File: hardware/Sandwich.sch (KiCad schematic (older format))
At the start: 2 parts

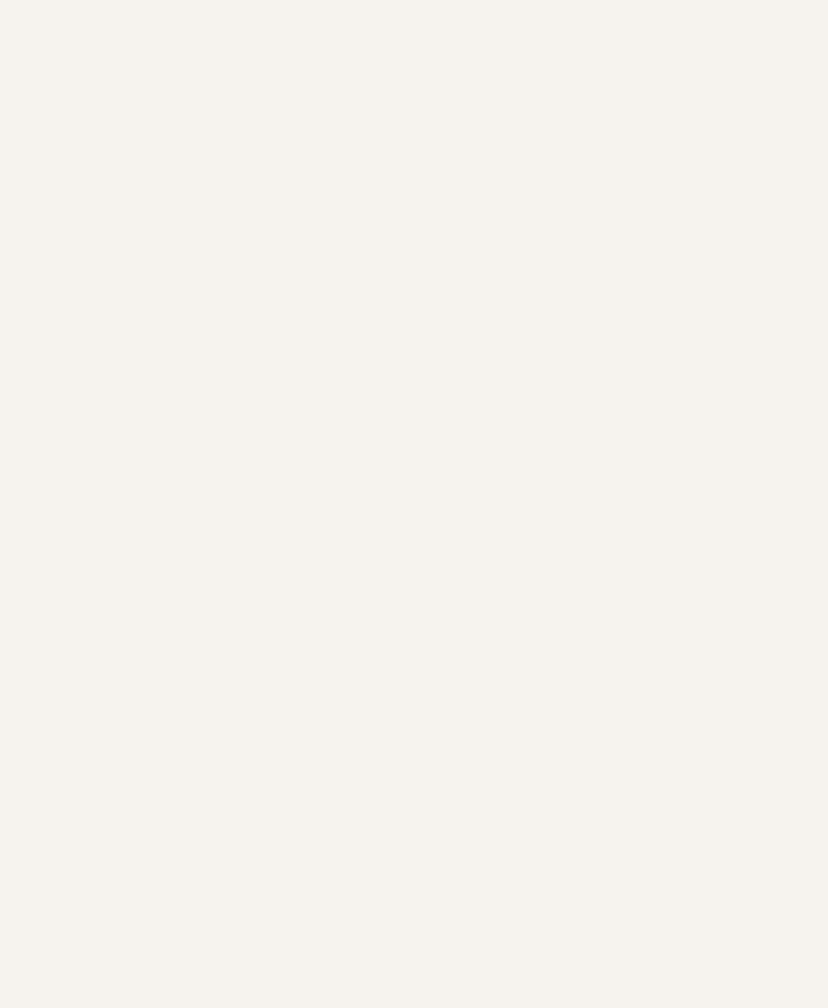
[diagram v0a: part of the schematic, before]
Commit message: Started working on the VGA interface.
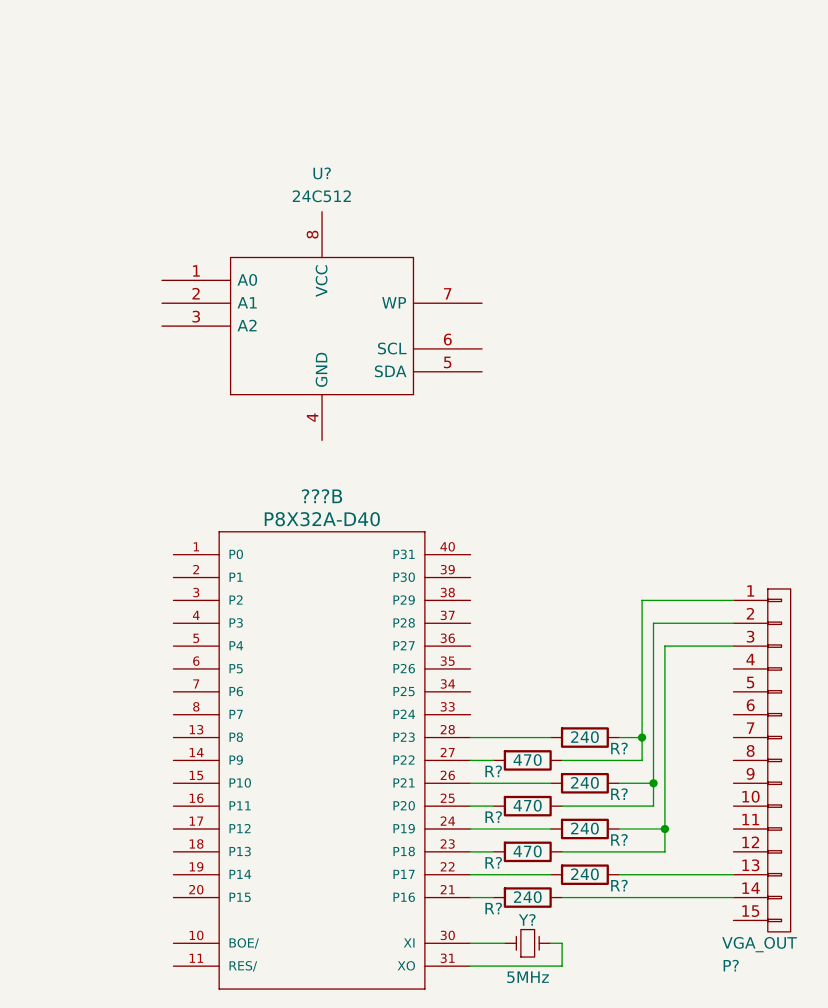
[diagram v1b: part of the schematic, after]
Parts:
- added ???: P8X32A-D40, symbol P8X32A-D40
- added P?: VGA_OUT, symbol CONN_01X15
- added R? (x5): 240, symbol R
- added R? (x3): 470, symbol R
- added U?: 24C512, symbol 24C512
- added Y?: 5MHz, symbol Crystal_Small
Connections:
- new net: ???.21 (P16), R?.2
- new net: ???.22 (P17), R?.2
- new net: ???.23 (P18), R?.2
- new net: ???.24 (P19), R?.2
- new net: ???.25 (P20), R?.2
- new net: ???.26 (P21), R?.2
- new net: ???.27 (P22), R?.2
- new net: ???.28 (P23), R?.2
- new net: ???.30 (XI), Y?.1
- new net: ???.31 (XO), Y?.2
- new net: P?.1 (P1), R?.1, R?.1
- new net: P?.13 (P13), R?.1
- new net: P?.14 (P14), R?.1
- new net: P?.2 (P2), R?.1, R?.1
- new net: P?.3 (P3), R?.1, R?.1
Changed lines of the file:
@@
 LIBS:valves
 LIBS:Zilog
+LIBS:parallax_propeller
+LIBS:Sandwich-cache
 EELAYER 25 0
 EELAYER END
@@
 Wire Wire Line
 	2100 5200 2300 5200
+$Comp
+L P8X32A-D40 ???
+U 2 1 56B3D7DA
+P 9050 4650
+F 0 "???" H 9100 5703 60  0000 C CNN
+F 1 "P8X32A-D40" H 9100 5603 60  0000 C CNN
+F 2 "" H 9050 4650 60  0000 C CNN
+F 3 "" H 9050 4650 60  0000 C CNN
+	2    9050 4650
+	1    0    0    -1
+$EndComp
+$Comp
+L CONN_01X15 P?
+U 1 1 56B3D8DB
+P 11100 4750
+F 0 "P?" H 10850 3850 50  0000 L CNN
+F 1 "VGA_OUT" H 10850 3950 50  0000 L CNN
+F 2 "" H 11100 4750 50  0000 C CNN
+F 3 "" H 11100 4750 50  0000 C CNN
+	1    11100 4750
+	1    0    0    -1
+$EndComp
+$Comp
+L R R?
+U 1 1 56B3DA31
+P 10000 5350
+F 0 "R?" V 10050 5200 50  0000 C CNN
+F 1 "240" V 10000 5350 50  0000 C CNN
+F 2 "" V 9930 5350 50  0000 C CNN
+F 3 "" H 10000 5350 50  0000 C CNN
+	1    10000 5350
+	0    1    1    0
+$EndComp
+$Comp
+L R R?
+U 1 1 56B3DA8C
+P 10250 5250
+F 0 "R?" V 10300 5400 50  0000 C CNN
+F 1 "240" V 10250 5250 50  0000 C CNN
+F 2 "" V 10180 5250 50  0000 C CNN
+F 3 "" H 10250 5250 50  0000 C CNN
+	1    10250 5250
+	0    1    1    0
+$EndComp
+Wire Wire Line
+	9750 5350 9850 5350
+Wire Wire Line
+	9750 5250 10100 5250
+$Comp
+L R R?
+U 1 1 56B3DB9A
+P 10000 5150
+F 0 "R?" V 10050 5000 50  0000 C CNN
+F 1 "470" V 10000 5150 50  0000 C CNN
+F 2 "" V 9930 5150 50  0000 C CNN
+F 3 "" H 10000 5150 50  0000 C CNN
+	1    10000 5150
+	0    1    1    0
+$EndComp
+$Comp
+L R R?
+U 1 1 56B3DBE5
+P 10250 5050
+F 0 "R?" V 10300 5200 50  0000 C CNN
+F 1 "240" V 10250 5050 50  0000 C CNN
+F 2 "" V 10180 5050 50  0000 C CNN
+F 3 "" H 10250 5050 50  0000 C CNN
+	1    10250 5050
+	0    1    1    0
+$EndComp
+Wire Wire Line
+	9850 5150 9750 5150
+Wire Wire Line
+	9750 5050 10100 5050
+$Comp
+L R R?
+U 1 1 56B3DEC9
+P 10000 4950
+F 0 "R?" V 10050 4800 50  0000 C CNN
+F 1 "470" V 10000 4950 50  0000 C CNN
+F 2 "" V 9930 4950 50  0000 C CNN
+F 3 "" H 10000 4950 50  0000 C CNN
+	1    10000 4950
+	0    1    1    0
+$EndComp
+$Comp
+L R R?
+U 1 1 56B3DF20
+P 10250 4850
+F 0 "R?" V 10300 5000 50  0000 C CNN
+F 1 "240" V 10250 4850 50  0000 C CNN
+F 2 "" V 10180 4850 50  0000 C CNN
+F 3 "" H 10250 4850 50  0000 C CNN
+	1    10250 4850
+	0    1    1    0
+$EndComp
+Wire Wire Line
+	9750 4950 9850 4950
+Wire Wire Line
+	10100 4850 9750 4850
+$Comp
+L R R?
+U 1 1 56B3E13C
+P 10000 4750
+F 0 "R?" V 10050 4600 50  0000 C CNN
+F 1 "470" V 10000 4750 50  0000 C CNN
+F 2 "" V 9930 4750 50  0000 C CNN
+F 3 "" H 10000 4750 50  0000 C CNN
+	1    10000 4750
+	0    1    1    0
+$EndComp
+$Comp
+L R R?
+U 1 1 56B3E18E
+P 10250 4650
+F 0 "R?" V 10300 4800 50  0000 C CNN
+F 1 "240" V 10250 4650 50  0000 C CNN
+F 2 "" V 10180 4650 50  0000 C CNN
+F 3 "" H 10250 4650 50  0000 C CNN
+	1    10250 4650
+	0    1    1    0
+$EndComp
+Wire Wire Line
+	9850 4750 9750 4750
+Wire Wire Line
+	9750 4650 10100 4650
+Wire Wire Line
+	10400 5250 10900 5250
+Wire Wire Line
+	10900 5350 10150 5350
+Wire Wire Line
+	10150 5150 10600 5150
+Wire Wire Line
+	10600 5150 10600 4250
+Wire Wire Line
+	10600 4250 10900 4250
+Wire Wire Line
+	10400 5050 10600 5050
+Connection ~ 10600 5050
+Wire Wire Line
+	10150 4950 10550 4950
+Wire Wire Line
+	10550 4950 10550 4150
+Wire Wire Line
+	10550 4150 10900 4150
+Wire Wire Line
+	10400 4850 10550 4850
+Connection ~ 10550 4850
+Wire Wire Line
+	10150 4750 10500 4750
+Wire Wire Line
+	10500 4750 10500 4050
+Wire Wire Line
+	10500 4050 10900 4050
+Wire Wire Line
+	10400 4650 10500 4650
+Connection ~ 10500 4650
+$Comp
+L Crystal_Small Y?
+U 1 1 56B3E76F
+P 10000 5550
+F 0 "Y?" H 10000 5650 50  0000 C CNN
+F 1 "5MHz" H 10000 5400 50  0000 C CNN
+F 2 "" H 10000 5550 50  0000 C CNN
+F 3 "" H 10000 5550 50  0000 C CNN
+	1    10000 5550
+	1    0    0    -1
+$EndComp
+Wire Wire Line
+	9750 5550 9900 5550
+Wire Wire Line
+	9750 5650 10150 5650
+Wire Wire Line
+	10150 5650 10150 5550
+Wire Wire Line
+	10150 5550 10100 5550
+$Comp
+L 24C512 U?
+U 1 1 56B3EA78
+P 9100 2850
+F 0 "U?" H 9100 3516 50  0000 C CNN
+F 1 "24C512" H 9100 3416 50  0000 C CNN
+F 2 "" H 9100 2850 50  0000 C CNN
+F 3 "" H 9100 2850 50  0000 C CNN
+	1    9100 2850
+	1    0    0    -1
+$EndComp
 $EndSCHEMATC

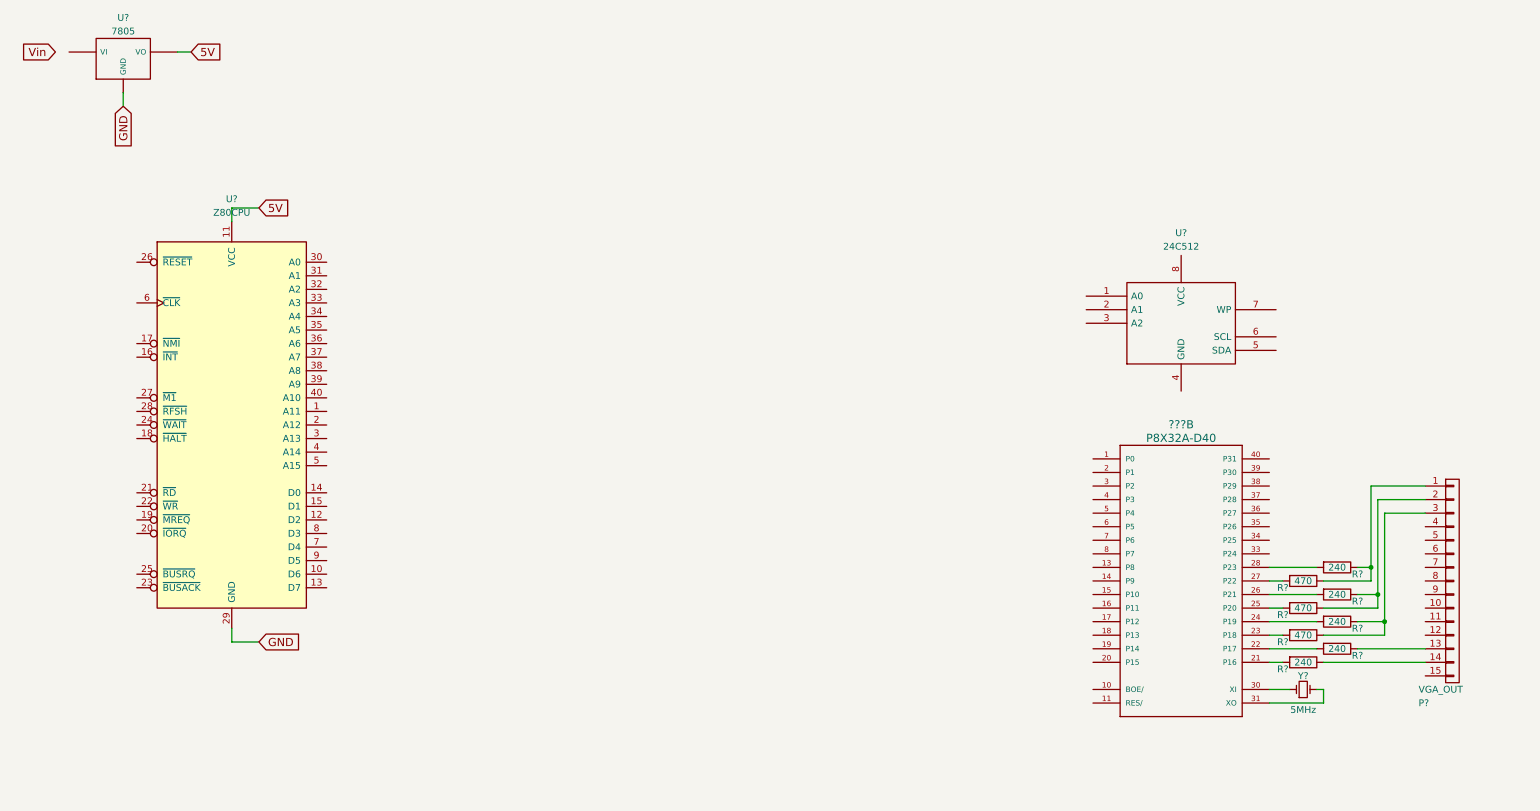
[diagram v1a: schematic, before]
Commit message: Added a circuit for resetting the Propeller for programming when DTR gets activated.
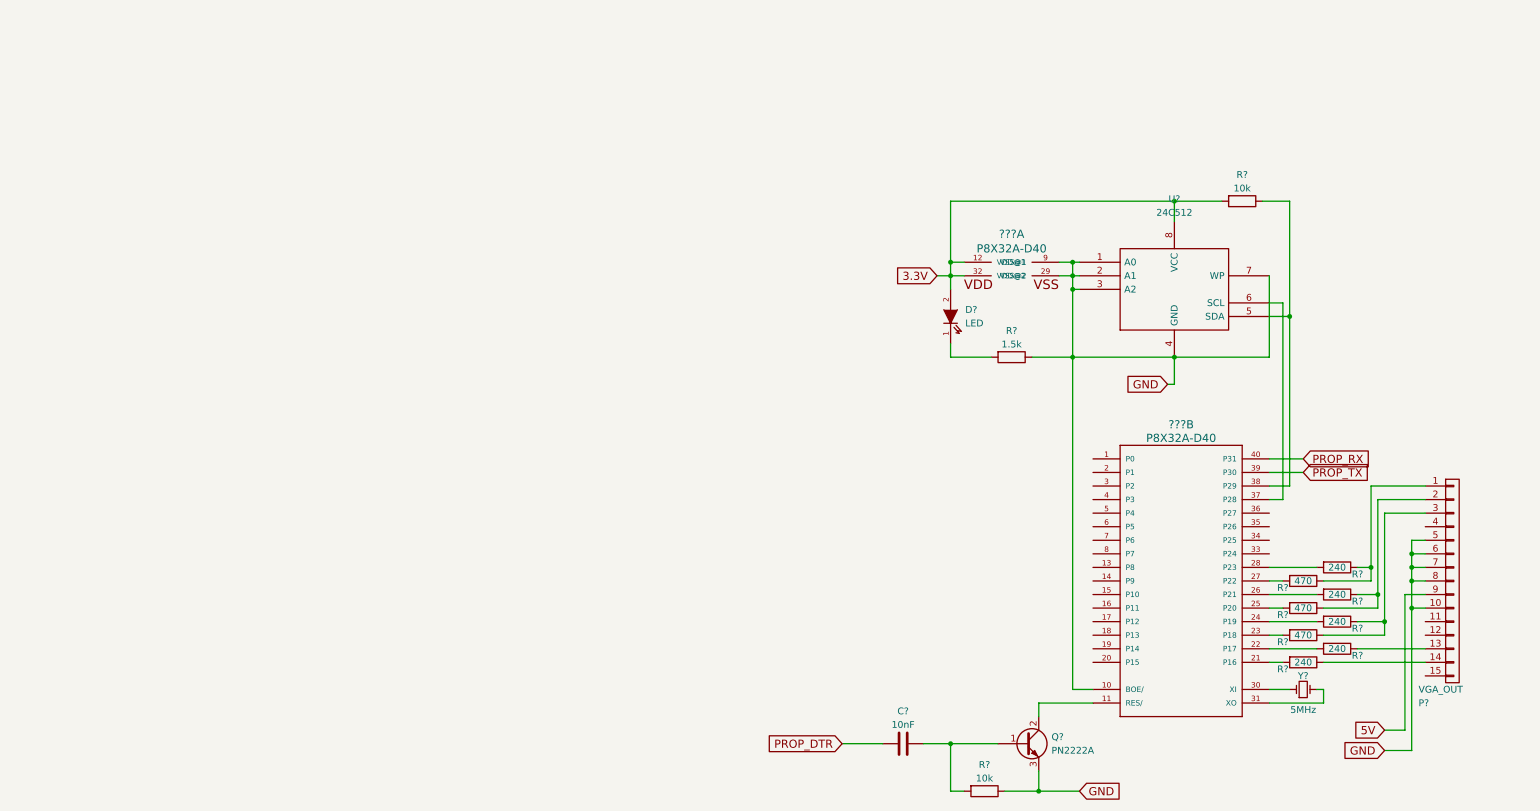
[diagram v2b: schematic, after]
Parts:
- removed U?: Z80CPU, symbol Z80CPU
- removed U?: 7805, symbol 7805
- added ???: P8X32A-D40, symbol P8X32A-D40
- added C?: 10nF, symbol C
- added D?: LED, symbol LED
- added Q?: PN2222A, symbol Q_NPN_BCE
- added R? (x2): 10k, symbol R
- added R?: 1.5k, symbol R
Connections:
- net 5V: now also P?.9 (P9)
- net GND: now also ???.10 (BOE/), P?.10 (P10), P?.5 (P5), P?.6 (P6), P?.7 (P7), P?.8 (P8), U?.1 (A0), U?.2 (A1), U?.3 (A2), U?.4 (GND), U?.7 (WP), ???.29 (VSS@2), ???.9 (VSS@1), Q?.3 (E), R?.1, R?.1
- net at ???.11 (RES/): now also Q?.2 (C)
- net at ???.37 (P28): now also U?.6 (SCL)
- net at ???.38 (P29): now also U?.5 (SDA), R?.1
- net PROP_TX: now reaches ???.39 (P30)
- net PROP_RX: now reaches ???.40 (P31)
- net 3.3V: now reaches U?.8 (VCC)
- net 3.3V: now also ???.12 (VDD@1), ???.32 (VDD@2), D?.2 (A), R?.2
- new net: D?.1 (K), R?.2
- new net: C?.1, Q?.1 (B), R?.2
- new net PROP_DTR: C?.2
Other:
- moved on the sheet: U?
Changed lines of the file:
@@
 $EndDescr
-$Comp
-L Z80CPU U?
-U 1 1 56AFD33E
-P 2100 3600
-F 0 "U?" H 2100 5266 50  0000 C CNN
-F 1 "Z80CPU" H 2100 5166 50  0000 C CNN
-F 2 "" H 2100 4000 50  0000 C CNN
-F 3 "" H 2100 4000 50  0000 C CNN
-	1    2100 3600
-	1    0    0    -1
-$EndComp
-$Comp
-L 7805 U?
-U 1 1 56AFD55A
-P 1300 900
-F 0 "U?" H 1300 1203 50  0000 C CNN
-F 1 "7805" H 1300 1103 50  0000 C CNN
-F 2 "" H 1300 900 50  0000 C CNN
-F 3 "" H 1300 900 50  0000 C CNN
-	1    1300 900
-	1    0    0    -1
-$EndComp
-Text GLabel 1800 850  2    60   Input ~ 0
-5V
-Text GLabel 1300 1250 3    60   Input ~ 0
-GND
-Text GLabel 800  850  0    60   Input ~ 0
-Vin
-Wire Wire Line
-	1700 850  1800 850
-Wire Wire Line
-	1300 1250 1300 1150
-Text GLabel 2300 2000 2    60   Input ~ 0
-5V
-Wire Wire Line
-	2100 2100 2100 2000
-Wire Wire Line
-	2100 2000 2300 2000
-Text GLabel 2300 5200 2    60   Input ~ 0
-GND
-Wire Wire Line
-	2100 5100 2100 5200
-Wire Wire Line
-	2100 5200 2300 5200
 $Comp
 L P8X32A-D40 ???
@@
 L 24C512 U?
 U 1 1 56B3EA78
-P 9100 2850
-F 0 "U?" H 9100 3516 50  0000 C CNN
-F 1 "24C512" H 9100 3416 50  0000 C CNN
-F 2 "" H 9100 2850 50  0000 C CNN
-F 3 "" H 9100 2850 50  0000 C CNN
-	1    9100 2850
-	1    0    0    -1
-$EndComp
+P 9050 2600
+F 0 "U?" H 9050 3266 50  0000 C CNN
+F 1 "24C512" H 9050 3166 50  0000 C CNN
+F 2 "" H 9050 2600 50  0000 C CNN
+F 3 "" H 9050 2600 50  0000 C CNN
+	1    9050 2600
+	1    0    0    -1
+$EndComp
+$Comp
+L P8X32A-D40 ???
+U 1 1 56B5DEF4
+P 7900 2600
+F 0 "???" H 7850 3008 60  0000 C CNN
+F 1 "P8X32A-D40" H 7850 2900 60  0000 C CNN
+F 2 "" H 7900 2600 60  0000 C CNN
+F 3 "" H 7900 2600 60  0000 C CNN
+	1    7900 2600
+	1    0    0    -1
+$EndComp
+Wire Wire Line
+	8350 2400 8200 2400
+Wire Wire Line
+	8200 2500 8350 2500
+Wire Wire Line
+	8000 3100 9750 3100
+Wire Wire Line
+	8300 2400 8300 5550
+Connection ~ 8300 2500
+Connection ~ 8300 2400
+Wire Wire Line
+	8350 2600 8300 2600
+Connection ~ 8300 2600
+Wire Wire Line
+	7300 2500 7500 2500
+Wire Wire Line
+	7400 1950 9400 1950
+Wire Wire Line
+	7500 2400 7400 2400
+Connection ~ 7400 2400
+Text GLabel 10600 6000 0    60   Input ~ 0
+GND
+Wire Wire Line
+	10600 6000 10800 6000
+Wire Wire Line
+	10800 6000 10800 4450
+Wire Wire Line
+	10800 4450 10900 4450
+Wire Wire Line
+	10900 4550 10800 4550
+Connection ~ 10800 4550
+Wire Wire Line
+	10900 4650 10800 4650
+Connection ~ 10800 4650
+Wire Wire Line
+	10900 4750 10800 4750
+Connection ~ 10800 4750
+Wire Wire Line
+	10900 4950 10800 4950
+Connection ~ 10800 4950
+Text GLabel 10600 5850 0    60   Input ~ 0
+5V
+Wire Wire Line
+	10600 5850 10750 5850
+Wire Wire Line
+	10750 5850 10750 4850
+Wire Wire Line
+	10750 4850 10900 4850
+$Comp
+L R R?
+U 1 1 56B5E9EC
+P 9550 1950
+F 0 "R?" V 9355 1950 50  0000 C CNN
+F 1 "10k" V 9455 1950 50  0000 C CNN
+F 2 "" V 9480 1950 50  0000 C CNN
+F 3 "" H 9550 1950 50  0000 C CNN
+	1    9550 1950
+	0    1    1    0
+$EndComp
+Connection ~ 9050 1950
+Wire Wire Line
+	9900 1950 9900 4050
+Wire Wire Line
+	9900 2800 9750 2800
+Wire Wire Line
+	9900 4050 9750 4050
+Connection ~ 9900 2800
+Wire Wire Line
+	9750 2700 9850 2700
+Wire Wire Line
+	9850 2700 9850 4150
+Wire Wire Line
+	9850 4150 9750 4150
+Wire Wire Line
+	9700 1950 9900 1950
+Connection ~ 7400 2500
+Text GLabel 9000 3300 0    60   Input ~ 0
+GND
+Wire Wire Line
+	9000 3300 9050 3300
+Wire Wire Line
+	9050 3300 9050 3100
+Text GLabel 7300 2500 0    60   Input ~ 0
+3.3V
+Wire Wire Line
+	7400 1950 7400 2600
+$Comp
+L LED D?
+U 1 1 56B5F331
+P 7400 2800
+F 0 "D?" V 7450 2692 50  0000 R CNN
+F 1 "LED" V 7350 2692 50  0000 R CNN
+F 2 "" H 7400 2800 50  0000 C CNN
+F 3 "" H 7400 2800 50  0000 C CNN
+	1    7400 2800
+	0    -1   -1   0
+$EndComp
+$Comp
+L R R?
+U 1 1 56B5F44A
+P 7850 3100
+F 0 "R?" V 7655 3100 50  0000 C CNN
+F 1 "1.5k" V 7755 3100 50  0000 C CNN
+F 2 "" V 7780 3100 50  0000 C CNN
+F 3 "" H 7850 3100 50  0000 C CNN
+	1    7850 3100
+	0    1    1    0
+$EndComp
+Wire Wire Line
+	7400 3000 7400 3100
+Wire Wire Line
+	7400 3100 7700 3100
+Connection ~ 8300 3100
+Wire Wire Line
+	9050 2100 9050 1950
+Wire Wire Line
+	9750 3100 9750 2500
+Connection ~ 9050 3100
+Text GLabel 10000 3850 2    60   Input ~ 0
+PROP_RX
+Text GLabel 10000 3950 2    60   Input ~ 0
+PROP_TX
+Wire Wire Line
+	10000 3850 9750 3850
+Wire Wire Line
+	9750 3950 10000 3950
+Wire Wire Line
+	8300 5550 8450 5550
+$Comp
+L R R?
+U 1 1 56B7C3FF
+P 7650 6300
+F 0 "R?" V 7455 6300 50  0000 C CNN
+F 1 "10k" V 7555 6300 50  0000 C CNN
+F 2 "" V 7580 6300 50  0000 C CNN
+F 3 "" H 7650 6300 50  0000 C CNN
+	1    7650 6300
+	0    1    1    0
+$EndComp
+$Comp
+L Q_NPN_BCE Q?
+U 1 1 56B7C5EC
+P 7950 5950
+F 0 "Q?" H 8144 6000 50  0000 L CNN
+F 1 "PN2222A" H 8144 5900 50  0000 L CNN
+F 2 "" H 8150 6050 50  0000 C CNN
+F 3 "" H 7950 5950 50  0000 C CNN
+	1    7950 5950
+	1    0    0    -1
+$EndComp
+Text GLabel 8350 6300 2    60   Input ~ 0
+GND
+Connection ~ 8050 6300
+Wire Wire Line
+	8050 5650 8450 5650
+Wire Wire Line
+	7800 6300 8350 6300
+Wire Wire Line
+	8050 6150 8050 6300
+Wire Wire Line
+	7500 6300 7400 6300
+Wire Wire Line
+	7400 6300 7400 5950
+Wire Wire Line
+	7200 5950 7750 5950
+Wire Wire Line
+	8050 5750 8050 5650
+$Comp
+L C C?
+U 1 1 56B7CB28
+P 7050 5950
+F 0 "C?" V 6810 5950 50  0000 C CNN
+F 1 "10nF" V 6910 5950 50  0000 C CNN
+F 2 "" H 7088 5800 50  0000 C CNN
+F 3 "" H 7050 5950 50  0000 C CNN
+	1    7050 5950
+	0    1    1    0
+$EndComp
+Text GLabel 6600 5950 0    60   Input ~ 0
+PROP_DTR
+Wire Wire Line
+	6600 5950 6900 5950
+Connection ~ 7400 5950
 $EndSCHEMATC
